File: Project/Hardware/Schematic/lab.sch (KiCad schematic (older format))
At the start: 29 parts, among them J1 USB_B_Micro, J2 6P Male, J3 Conn_01x03_Male, U2 STM32F411RETx, U3 NCP1117-3.3_SOT223, Y1 8MHz

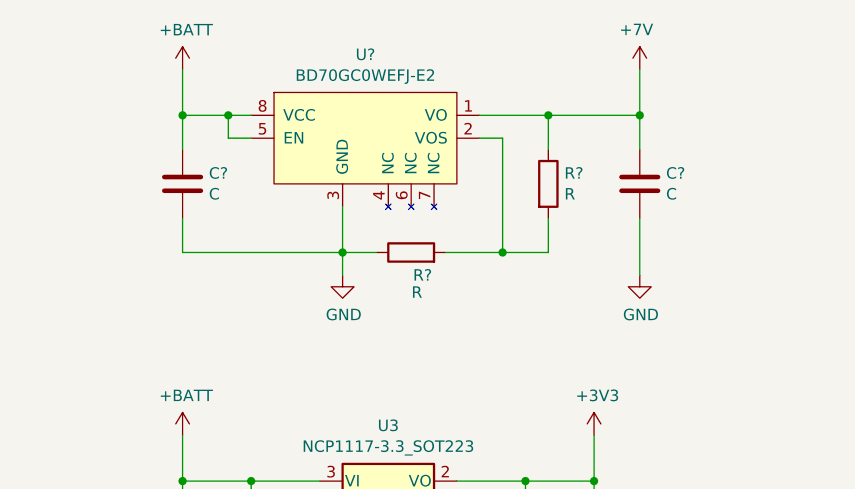
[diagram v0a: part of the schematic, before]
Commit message: Korrigerade 7-voltsregulatorn: det är fixed, inte adjustable.
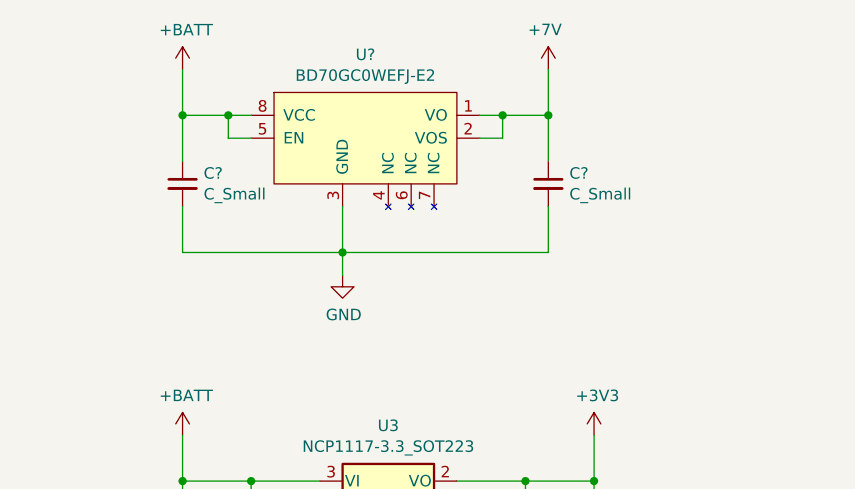
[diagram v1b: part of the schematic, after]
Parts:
- removed C? (x2): C, symbol Device:C
- removed R? (x2): R, symbol Device:R
- added C? (x2): C_Small, symbol Device:C_Small
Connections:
- net +7V: now also U?.2 (VOS), C?.1
- net +BATT: now also C?.1
- net GND: now also C?.2, C?.2
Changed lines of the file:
@@
 Wire Wire Line
 	2600 1100 2700 1100
-$Comp
-L Device:C C?
-U 1 1 5C6012C4
-P 2400 1400
-F 0 "C?" H 2515 1446 50  0000 L CNN
-F 1 "C" H 2515 1355 50  0000 L CNN
-F 2 "" H 2438 1250 50  0001 C CNN
-F 3 "~" H 2400 1400 50  0001 C CNN
-	1    2400 1400
-	1    0    0    -1
-$EndComp
-Wire Wire Line
-	2400 1250 2400 1100
 Wire Wire Line
 	2400 1100 2600 1100
 Connection ~ 2600 1100
-$Comp
-L Device:R R?
-U 1 1 5C615406
-P 3400 1700
-F 0 "R?" V 3300 1650 50  0000 C CNN
-F 1 "R" V 3225 1675 50  0000 C CNN
-F 2 "" V 3330 1700 50  0001 C CNN
-F 3 "~" H 3400 1700 50  0001 C CNN
-	1    3400 1700
-	0    -1   -1   0
-$EndComp
-$Comp
-L Device:C C?
-U 1 1 5C6157A1
-P 4400 1400
-F 0 "C?" H 4515 1446 50  0000 L CNN
-F 1 "C" H 4515 1355 50  0000 L CNN
-F 2 "" H 4438 1250 50  0001 C CNN
-F 3 "~" H 4400 1400 50  0001 C CNN
-	1    4400 1400
-	1    0    0    -1
-$EndComp
-Wire Wire Line
-	4400 1250 4400 1100
-Wire Wire Line
-	3250 1700 3100 1700
-Wire Wire Line
-	4000 1550 4000 1700
-Wire Wire Line
-	3550 1700 3800 1700
-Wire Wire Line
-	3700 1100 4000 1100
-$Comp
-L Device:R R?
-U 1 1 5C6153A2
-P 4000 1400
-F 0 "R?" H 4070 1446 50  0000 L CNN
-F 1 "R" H 4070 1355 50  0000 L CNN
-F 2 "" V 3930 1400 50  0001 C CNN
-F 3 "~" H 4000 1400 50  0001 C CNN
-	1    4000 1400
-	1    0    0    -1
-$EndComp
-Wire Wire Line
-	4000 1250 4000 1100
-Connection ~ 4000 1100
-Wire Wire Line
-	4400 1100 4000 1100
 Wire Wire Line
 	3100 1700 3100 1500
-Wire Wire Line
-	3800 1700 3800 1200
-Wire Wire Line
-	3800 1200 3700 1200
-Connection ~ 3800 1700
-Wire Wire Line
-	3800 1700 4000 1700
 $Comp
 L power:GND #PWR?
@@
 Wire Wire Line
 	2400 1700 3100 1700
-Wire Wire Line
-	2400 1550 2400 1700
 $Comp
-L power:GND #PWR?
-U 1 1 5C6D4879
-P 4400 1800
-F 0 "#PWR?" H 4400 1550 50  0001 C CNN
-F 1 "GND" H 4405 1627 50  0000 C CNN
-F 2 "" H 4400 1800 50  0001 C CNN
-F 3 "" H 4400 1800 50  0001 C CNN
-	1    4400 1800
+L PASC:+7V #PWR?
+U 1 1 5C6FF278
+P 4000 900
+F 0 "#PWR?" H 4250 1000 50  0001 C CNN
+F 1 "+7V" H 3985 1074 50  0000 C CNN
+F 2 "" H 4000 900 50  0001 C CNN
+F 3 "" H 4000 900 50  0001 C CNN
+	1    4000 900
 	1    0    0    -1
 $EndComp
 Wire Wire Line
-	4400 1550 4400 1800
-$Comp
-L PASC:+7V #PWR?
-U 1 1 5C6FF278
-P 4400 900
-F 0 "#PWR?" H 4650 1000 50  0001 C CNN
-F 1 "+7V" H 4385 1074 50  0000 C CNN
-F 2 "" H 4400 900 50  0001 C CNN
-F 3 "" H 4400 900 50  0001 C CNN
-	1    4400 900
-	1    0    0    -1
-$EndComp
-Wire Wire Line
-	4400 1100 4400 900
-Connection ~ 4400 1100
+	4000 1100 4000 900
+Connection ~ 4000 1100
 $Comp
 L power:+BATT #PWR?
@@
 	2400 900  2400 1100
 Connection ~ 2400 1100
+Wire Wire Line
+	3100 1700 4000 1700
+Wire Wire Line
+	3700 1100 3800 1100
+Wire Wire Line
+	3700 1200 3800 1200
+Wire Wire Line
+	3800 1200 3800 1100
+Connection ~ 3800 1100
+Wire Wire Line
+	3800 1100 4000 1100
+$Comp
+L Device:C_Small C?
+U 1 1 5C75A786
+P 2400 1400
+F 0 "C?" H 2492 1446 50  0000 L CNN
+F 1 "C_Small" H 2492 1355 50  0000 L CNN
+F 2 "" H 2400 1400 50  0001 C CNN
+F 3 "~" H 2400 1400 50  0001 C CNN
+	1    2400 1400
+	1    0    0    -1
+$EndComp
+$Comp
+L Device:C_Small C?
+U 1 1 5C75A7D6
+P 4000 1400
+F 0 "C?" H 4092 1446 50  0000 L CNN
+F 1 "C_Small" H 4092 1355 50  0000 L CNN
+F 2 "" H 4000 1400 50  0001 C CNN
+F 3 "~" H 4000 1400 50  0001 C CNN
+	1    4000 1400
+	1    0    0    -1
+$EndComp
+Wire Wire Line
+	4000 1100 4000 1300
+Wire Wire Line
+	4000 1500 4000 1700
+Wire Wire Line
+	2400 1500 2400 1700
+Wire Wire Line
+	2400 1100 2400 1300
 $EndSCHEMATC

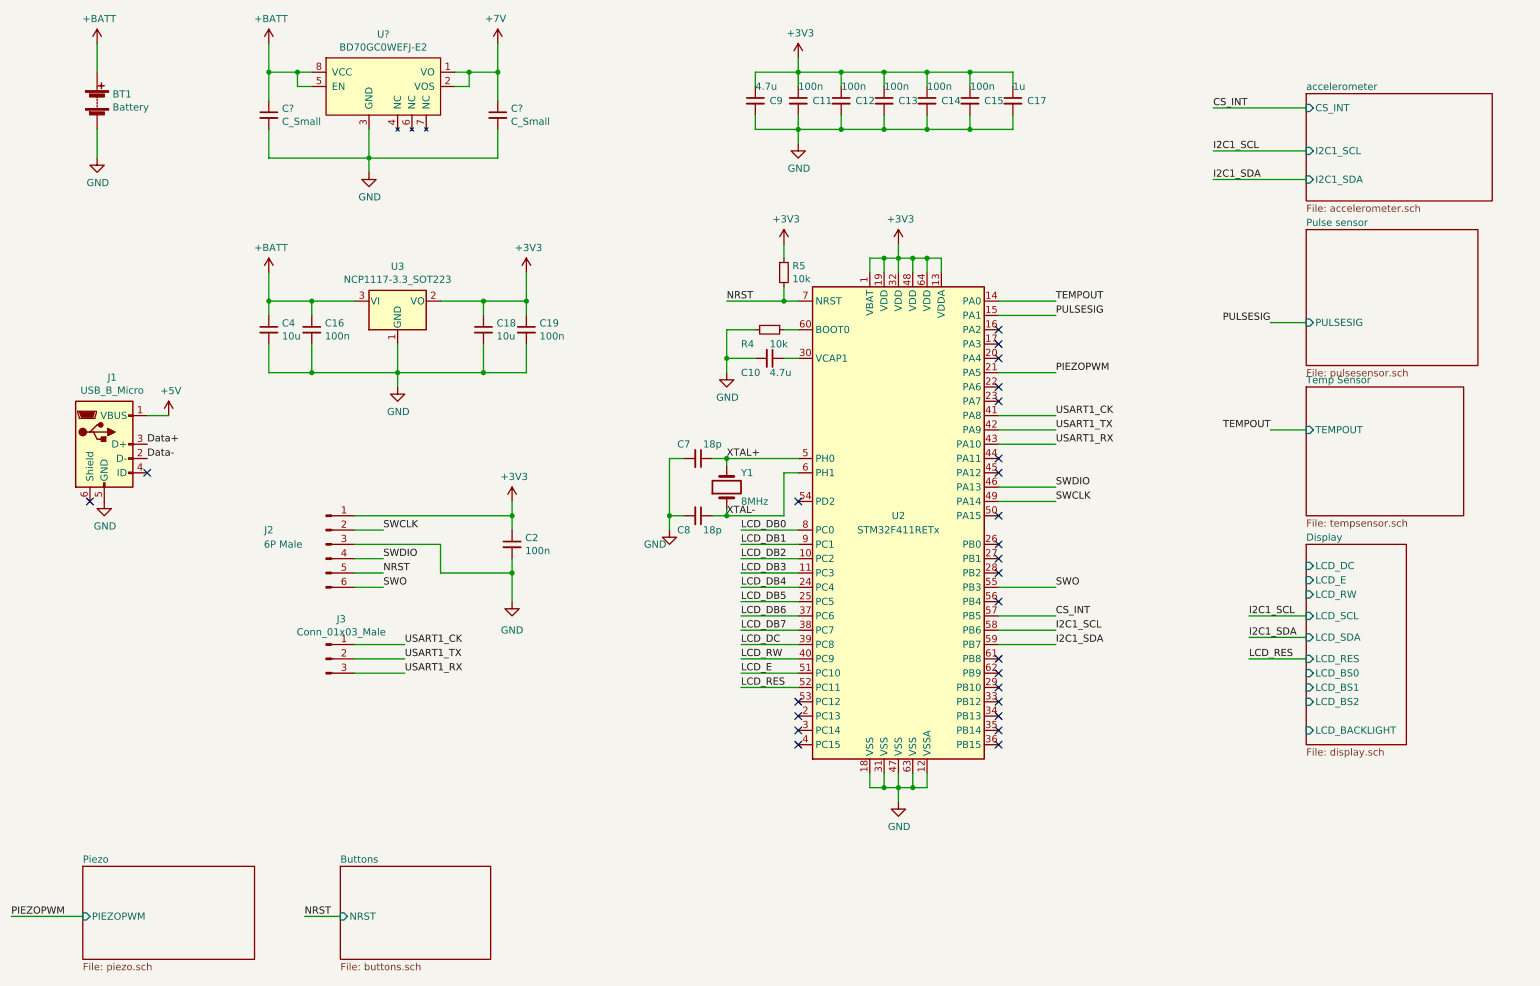
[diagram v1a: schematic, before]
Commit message: La till en till display och fixa fel
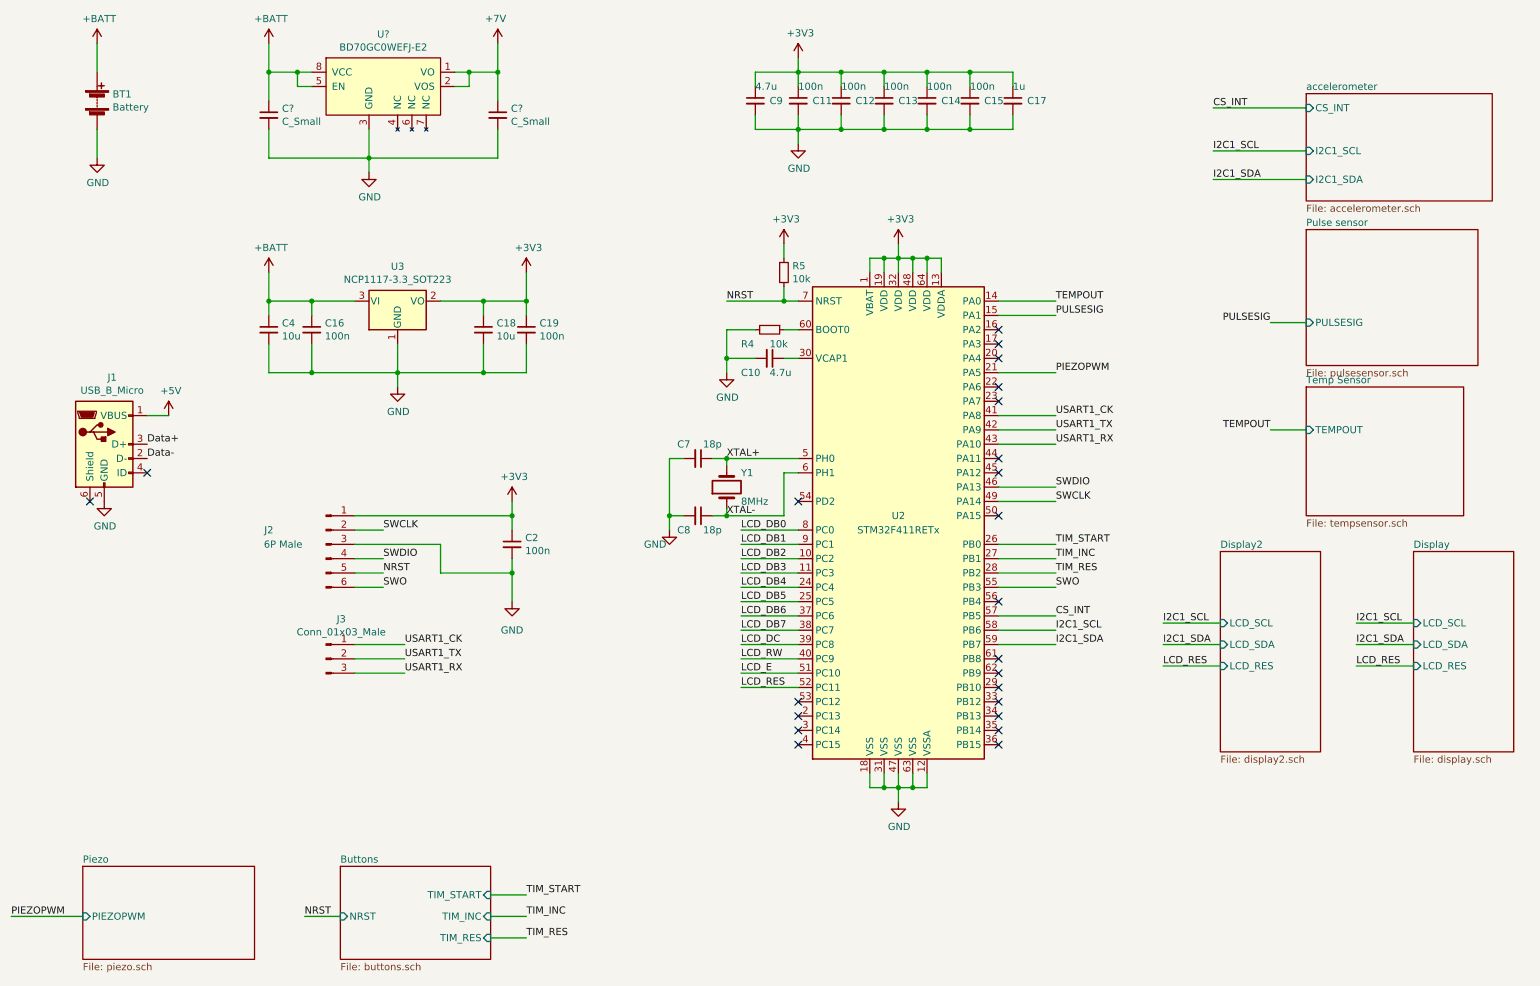
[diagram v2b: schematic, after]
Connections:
- net TIM_START: now reaches U2.26 (PB0)
- net TIM_INC: now reaches U2.27 (PB1)
- net TIM_RES: now reaches U2.28 (PB2)
- no-connect marks 26 -> 23
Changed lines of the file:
@@
 $Descr A4 11693 8268
 encoding utf-8
-Sheet 1 7
+Sheet 1 8
 Title ""
 Date ""
@@
 NoConn ~ 7500 3900
 NoConn ~ 7500 4200
-NoConn ~ 7500 4400
-NoConn ~ 7500 4600
-NoConn ~ 7500 4500
 NoConn ~ 7500 4800
 NoConn ~ 7500 5500
@@
 $EndSheet
 $Sheet
-S 9650 4400 700  1400
+S 10400 4450 700  1400
 U 5C564F2E
 F0 "Display" 50
 F1 "display.sch" 50
-F2 "LCD_BACKLIGHT" I L 9650 5700 50
-F3 "LCD_RW" I L 9650 4750 50
-F4 "LCD_E" I L 9650 4650 50
-F5 "LCD_BS0" I L 9650 5300 50
-F6 "LCD_BS1" I L 9650 5400 50
-F7 "LCD_BS2" I L 9650 5500 50
-F8 "LCD_RES" I L 9650 5200 50
-F9 "LCD_DC" I L 9650 4550 50
-F10 "LCD_SDA" I L 9650 5050 50
-F11 "LCD_SCL" I L 9650 4900 50
+F8 "LCD_RES" I L 10400 5250 50
+F10 "LCD_SDA" I L 10400 5100 50
+F11 "LCD_SCL" I L 10400 4950 50
 $EndSheet
 $Sheet
@@
 F1 "buttons.sch" 50
 F2 "NRST" I L 2900 7000 50
+F3 "TIM_START" I R 3950 6850 50
+F4 "TIM_INC" I R 3950 7000 50
+F5 "TIM_RES" I R 3950 7150 50
 $EndSheet
 $Comp
@@
 NoConn ~ 6100 5500
 Wire Wire Line
-	9650 5050 9250 5050
-Text Label 9250 5050 0    50   ~ 0
+	10400 5100 10000 5100
+Text Label 10000 5100 0    50   ~ 0
 I2C1_SDA
 Wire Wire Line
-	9650 4900 9250 4900
-Text Label 9250 4900 0    50   ~ 0
+	10400 4950 10000 4950
+Text Label 10000 4950 0    50   ~ 0
 I2C1_SCL
-Text Label 9250 5200 0    50   ~ 0
+Text Label 10000 5250 0    50   ~ 0
 LCD_RES
 Wire Wire Line
-	9250 5200 9650 5200
+	10000 5250 10400 5250
 $Comp
 L PASC:BD70GC0WEFJ-E2 U?
@@
 Wire Wire Line
 	2400 1100 2400 1300
+$Sheet
+S 9050 4450 700  1400
+U 5C5FFA20
+F0 "Display2" 50
+F1 "display2.sch" 50
+F8 "LCD_RES" I L 9050 5250 50
+F10 "LCD_SDA" I L 9050 5100 50
+F11 "LCD_SCL" I L 9050 4950 50
+$EndSheet
+Wire Wire Line
+	9050 5100 8650 5100
+Text Label 8650 5100 0    50   ~ 0
+I2C1_SDA
+Wire Wire Line
+	9050 4950 8650 4950
+Text Label 8650 4950 0    50   ~ 0
+I2C1_SCL
+Text Label 8650 5250 0    50   ~ 0
+LCD_RES
+Wire Wire Line
+	8650 5250 9050 5250
+Wire Wire Line
+	3950 6850 4200 6850
+Text Label 4200 6850 0    50   ~ 0
+TIM_START
+Wire Wire Line
+	3950 7000 4200 7000
+Text Label 4200 7000 0    50   ~ 0
+TIM_INC
+Wire Wire Line
+	3950 7150 4200 7150
+Text Label 4200 7150 0    50   ~ 0
+TIM_RES
+Text Label 7900 4600 0    50   ~ 0
+TIM_RES
+Text Label 7900 4400 0    50   ~ 0
+TIM_START
+Text Label 7900 4500 0    50   ~ 0
+TIM_INC
+Wire Wire Line
+	7500 4400 7900 4400
+Wire Wire Line
+	7500 4500 7900 4500
+Wire Wire Line
+	7500 4600 7900 4600
 $EndSCHEMATC

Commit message: Byta skärm, igen igen (#11)
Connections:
- net LCD_DB2 is gone; now on net LCD_DC: U2.10 (PC2)
- net LCD_DC: no longer U2.39 (PC8)
- net PIEZOPWM: now also U2.50 (PA15); no longer U2.21 (PA5)
- net TIM3_CH1: now reaches U2.22 (PA6)
- net SPI1_MOSI: now reaches U2.23 (PA7)
- net LCD_DB0 renamed LCD_SCE
- net LCD_DB1 renamed LCD_RST
- net LCD_DB3: no longer names the net of U2.11 (PC3)
- net LCD_DB4: no longer names the net of U2.24 (PC4)
- net LCD_DB5: no longer names the net of U2.25 (PC5)
- net LCD_DB6: no longer names the net of U2.37 (PC6)
- net LCD_DB7: no longer names the net of U2.38 (PC7)
- net LCD_E: no longer names the net of U2.51 (PC10)
- net LCD_RES: no longer names the net of U2.52 (PC11)
- net LCD_RW: no longer names the net of U2.40 (PC9)
- new net SPI1_SCK: U2.21 (PA5)
- no-connect marks 23 -> 29
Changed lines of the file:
@@
 $Descr A4 11693 8268
 encoding utf-8
-Sheet 1 8
+Sheet 1 7
 Title ""
 Date ""
@@
 NoConn ~ 7500 3000
 NoConn ~ 7500 3100
-NoConn ~ 7500 3300
-NoConn ~ 7500 3400
 NoConn ~ 7500 3800
 NoConn ~ 7500 3900
-NoConn ~ 7500 4200
 NoConn ~ 7500 4800
 NoConn ~ 7500 5500
@@
 $EndSheet
 $Sheet
-S 10400 4450 700  1400
+S 9650 4550 700  1400
 U 5C564F2E
 F0 "Display" 50
 F1 "display.sch" 50
-F8 "LCD_RES" I L 10400 5250 50
-F10 "LCD_SDA" I L 10400 5100 50
-F11 "LCD_SCL" I L 10400 4950 50
+F2 "LCD_LED" I L 9650 4750 50
+F3 "LCD_DN" I L 9650 5400 50
+F4 "LCD_SCE" I L 9650 4900 50
+F5 "LCD_RST" I L 9650 5050 50
+F6 "LCD_DC" I L 9650 5200 50
+F7 "LCD_SCK" I L 9650 5550 50
 $EndSheet
 $Sheet
@@
 Text Label 7900 2700 0    50   ~ 0
 TEMPOUT
-Wire Wire Line
-	7500 3200 7900 3200
-Text Label 7900 3200 0    50   ~ 0
-PIEZOPWM
 $Comp
 L Connector:Conn_01x03_Male J3
@@
 Text Label 3350 5300 0    50   ~ 0
 USART1_RX
-Text Label 5700 4400 0    50   ~ 0
-LCD_DB1
-Text Label 5700 4500 0    50   ~ 0
-LCD_DB2
-Wire Wire Line
-	5700 4300 6100 4300
-Wire Wire Line
-	5700 4400 6100 4400
-Wire Wire Line
-	5700 4500 6100 4500
-Wire Wire Line
-	6100 4600 5700 4600
-Text Label 5700 4600 0    50   ~ 0
-LCD_DB3
-Wire Wire Line
-	6100 4700 5700 4700
-Text Label 5700 4700 0    50   ~ 0
-LCD_DB4
-Wire Wire Line
-	6100 4800 5700 4800
-Text Label 5700 4800 0    50   ~ 0
-LCD_DB5
-Text Label 5700 4900 0    50   ~ 0
-LCD_DB6
-Text Label 5700 5000 0    50   ~ 0
-LCD_DB7
-Wire Wire Line
-	5700 4900 6100 4900
-Wire Wire Line
-	5700 5000 6100 5000
-Wire Wire Line
-	6100 5100 5700 5100
-Text Label 5700 5100 0    50   ~ 0
-LCD_DC
-Wire Wire Line
-	6100 5200 5700 5200
-Text Label 5700 5200 0    50   ~ 0
-LCD_RW
-Wire Wire Line
-	6100 5300 5700 5300
-Text Label 5700 5300 0    50   ~ 0
-LCD_E
 $Comp
 L Connector:USB_B_Micro J1
@@
 CS_INT
 NoConn ~ 7500 5400
-Text Label 5700 5400 0    50   ~ 0
-LCD_RES
-Wire Wire Line
-	6100 5400 5700 5400
 Wire Wire Line
 	9650 2850 9400 2850
@@
 Text Label 2650 7000 0    50   ~ 0
 NRST
-Text Label 5700 4300 0    50   ~ 0
-LCD_DB0
 NoConn ~ 6100 5500
-Wire Wire Line
-	10400 5100 10000 5100
-Text Label 10000 5100 0    50   ~ 0
-I2C1_SDA
-Wire Wire Line
-	10400 4950 10000 4950
-Text Label 10000 4950 0    50   ~ 0
-I2C1_SCL
-Text Label 10000 5250 0    50   ~ 0
-LCD_RES
-Wire Wire Line
-	10000 5250 10400 5250
 $Comp
 L PASC:BD70GC0WEFJ-E2 U?
@@
 Wire Wire Line
 	2400 1100 2400 1300
-$Sheet
-S 9050 4450 700  1400
-U 5C5FFA20
-F0 "Display2" 50
-F1 "display2.sch" 50
-F8 "LCD_RES" I L 9050 5250 50
-F10 "LCD_SDA" I L 9050 5100 50
-F11 "LCD_SCL" I L 9050 4950 50
-$EndSheet
-Wire Wire Line
-	9050 5100 8650 5100
-Text Label 8650 5100 0    50   ~ 0
-I2C1_SDA
-Wire Wire Line
-	9050 4950 8650 4950
-Text Label 8650 4950 0    50   ~ 0
-I2C1_SCL
-Text Label 8650 5250 0    50   ~ 0
-LCD_RES
-Wire Wire Line
-	8650 5250 9050 5250
 Wire Wire Line
 	3950 6850 4200 6850
@@
 Wire Wire Line
 	7500 4600 7900 4600
+Wire Wire Line
+	7500 3200 7900 3200
+Text Label 7900 3200 0    50   ~ 0
+SPI1_SCK
+Text Label 9650 5550 2    50   ~ 0
+SPI1_SCK
+Wire Wire Line
+	7500 3400 7900 3400
+Text Label 7900 3400 0    50   ~ 0
+SPI1_MOSI
+Text Label 9650 5400 2    50   ~ 0
+SPI1_MOSI
+Text Label 6100 4300 2    50   ~ 0
+LCD_SCE
+Text Label 6100 4400 2    50   ~ 0
+LCD_RST
+Text Label 6100 4500 2    50   ~ 0
+LCD_DC
+Text Label 9650 4900 2    50   ~ 0
+LCD_SCE
+Text Label 9650 5050 2    50   ~ 0
+LCD_RST
+Text Label 9650 5200 2    50   ~ 0
+LCD_DC
+Wire Wire Line
+	7500 3300 7900 3300
+Text Label 7900 3300 0    50   ~ 0
+TIM3_CH1
+Text Label 9650 4750 2    50   ~ 0
+TIM3_CH1
+Wire Wire Line
+	7500 4200 7900 4200
+Text Label 7900 4200 0    50   ~ 0
+PIEZOPWM
+NoConn ~ 6100 4600
+NoConn ~ 6100 4700
+NoConn ~ 6100 4800
+NoConn ~ 6100 4900
+NoConn ~ 6100 5000
+NoConn ~ 6100 5100
+NoConn ~ 6100 5200
+NoConn ~ 6100 5300
+NoConn ~ 6100 5400
 $EndSCHEMATC
